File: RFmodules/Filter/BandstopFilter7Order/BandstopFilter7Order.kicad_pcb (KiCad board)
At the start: 2 copper layers, 26.8 x 9.2 mm, 17 parts, among them J1 SMA, J2 SMA

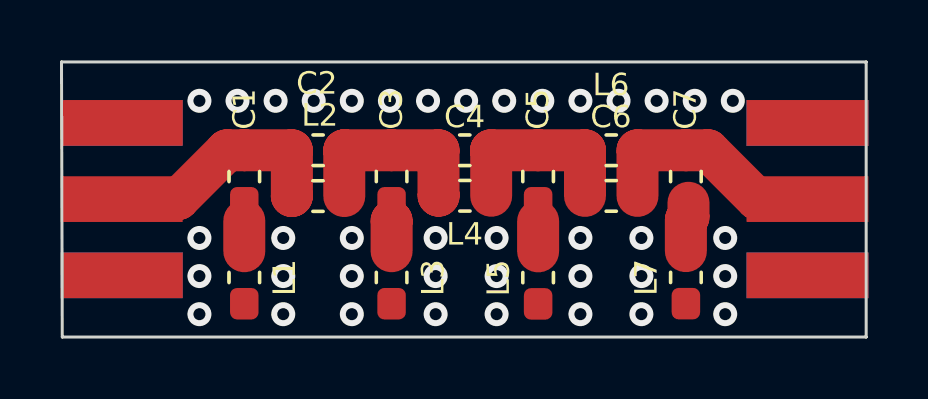
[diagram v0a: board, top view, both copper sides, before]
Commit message: Fix design guide issues
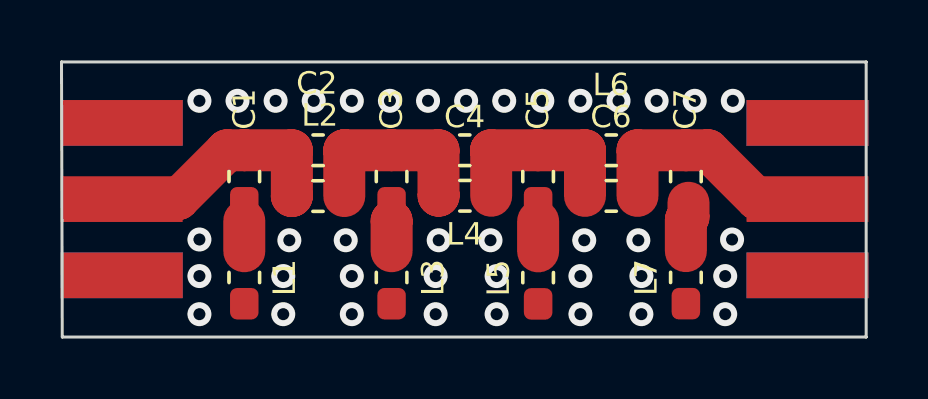
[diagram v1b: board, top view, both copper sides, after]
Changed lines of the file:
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@@
   (layers
     (0 F.Cu signal)
-    (31 B.Cu signal hide)
+    (31 B.Cu signal)
     (32 B.Adhes user)
     (33 F.Adhes user)
@@
     (last_trace_width 0.25)
     (trace_clearance 0.2)
-    (zone_clearance 0.2)
+    (zone_clearance 0.1)
     (zone_45_only no)
     (trace_min 0.2)
@@
   (gr_line (start 130.4798 96.2152) (end 130.4798 105.3846) (layer Edge.Cuts) (width 0.1))
   (gr_line (start 103.6574 96.2152) (end 130.4798 96.2152) (layer Edge.Cuts) (width 0.1))
-  (via (at 113.3348 102.0826) (size 0.8) (drill 0.4) (layers F.Cu B.Cu) (net 9))
-  (via (at 116.1288 102.0826) (size 0.8) (drill 0.4) (layers F.Cu B.Cu) (net 9))
-  (via (at 118.1608 102.0826) (size 0.8) (drill 0.4) (layers F.Cu B.Cu) (net 9))
-  (via (at 120.9548 102.0826) (size 0.8) (drill 0.4) (layers F.Cu B.Cu) (net 9))
-  (via (at 122.9868 102.0826) (size 0.8) (drill 0.4) (layers F.Cu B.Cu) (net 9))
-  (via (at 113.3348 104.6226) (size 0.8) (drill 0.4) (layers F.Cu B.Cu) (net 9))
-  (via (at 113.3348 103.3526) (size 0.8) (drill 0.4) (layers F.Cu B.Cu) (net 9))
-  (via (at 116.1288 103.3526) (size 0.8) (drill 0.4) (layers F.Cu B.Cu) (net 9))
-  (via (at 116.1288 104.6226) (size 0.8) (drill 0.4) (layers F.Cu B.Cu) (net 9))
-  (via (at 118.1608 103.3526) (size 0.8) (drill 0.4) (layers F.Cu B.Cu) (net 9))
-  (via (at 118.1608 104.6226) (size 0.8) (drill 0.4) (layers F.Cu B.Cu) (net 9))
-  (via (at 120.9548 103.3526) (size 0.8) (drill 0.4) (layers F.Cu B.Cu) (net 9))
-  (via (at 120.9548 104.6226) (size 0.8) (drill 0.4) (layers F.Cu B.Cu) (net 9))
-  (via (at 122.9868 103.3526) (size 0.8) (drill 0.4) (layers F.Cu B.Cu) (net 9))
-  (via (at 122.9868 104.6226) (size 0.8) (drill 0.4) (layers F.Cu B.Cu) (net 9))
-  (via (at 108.2548 103.3526) (size 0.8) (drill 0.4) (layers F.Cu B.Cu) (net 9))
-  (via (at 108.2548 102.0826) (size 0.8) (drill 0.4) (layers F.Cu B.Cu) (net 9))
-  (via (at 125.7808 102.0826) (size 0.8) (drill 0.4) (layers F.Cu B.Cu) (net 9))
-  (via (at 125.7808 103.3526) (size 0.8) (drill 0.4) (layers F.Cu B.Cu) (net 9))
-  (via (at 125.7808 104.6226) (size 0.8) (drill 0.4) (layers F.Cu B.Cu) (net 9))
-  (via (at 111.0488 104.6226) (size 0.8) (drill 0.4) (layers F.Cu B.Cu) (net 9))
-  (via (at 111.0488 103.3526) (size 0.8) (drill 0.4) (layers F.Cu B.Cu) (net 9))
-  (via (at 111.0488 102.0826) (size 0.8) (drill 0.4) (layers F.Cu B.Cu) (net 9))
   (segment (start 109.75086 99.15906) (end 111.33582 99.15906) (width 1.4) (layer F.Cu) (net 1) (status 30))
   (segment (start 111.33582 100.68312) (end 111.33334 100.6856) (width 1.4) (layer F.Cu) (net 1) (status 30))
@@
   (segment (start 124.47016 101.471737) (end 124.55721 101.384687) (width 1.4) (layer F.Cu) (net 8))
   (segment (start 124.47016 102.52202) (end 124.47016 101.471737) (width 1.4) (layer F.Cu) (net 8))
+  (via (at 113.1316 102.1588) (size 0.8) (drill 0.4) (layers F.Cu B.Cu) (net 9))
+  (via (at 116.2304 102.1588) (size 0.8) (drill 0.4) (layers F.Cu B.Cu) (net 9))
+  (via (at 117.9576 102.1588) (size 0.8) (drill 0.4) (layers F.Cu B.Cu) (net 9))
+  (via (at 121.0818 102.1588) (size 0.8) (drill 0.4) (layers F.Cu B.Cu) (net 9))
+  (via (at 122.8852 102.1588) (size 0.8) (drill 0.4) (layers F.Cu B.Cu) (net 9))
+  (via (at 113.3348 104.6226) (size 0.8) (drill 0.4) (layers F.Cu B.Cu) (net 9))
+  (via (at 113.3348 103.3526) (size 0.8) (drill 0.4) (layers F.Cu B.Cu) (net 9))
+  (via (at 116.1288 103.3526) (size 0.8) (drill 0.4) (layers F.Cu B.Cu) (net 9))
+  (via (at 116.1288 104.6226) (size 0.8) (drill 0.4) (layers F.Cu B.Cu) (net 9))
+  (via (at 118.1608 103.3526) (size 0.8) (drill 0.4) (layers F.Cu B.Cu) (net 9))
+  (via (at 118.1608 104.6226) (size 0.8) (drill 0.4) (layers F.Cu B.Cu) (net 9))
+  (via (at 120.9548 103.3526) (size 0.8) (drill 0.4) (layers F.Cu B.Cu) (net 9))
+  (via (at 120.9548 104.6226) (size 0.8) (drill 0.4) (layers F.Cu B.Cu) (net 9))
+  (via (at 122.9868 103.3526) (size 0.8) (drill 0.4) (layers F.Cu B.Cu) (net 9))
+  (via (at 122.9868 104.6226) (size 0.8) (drill 0.4) (layers F.Cu B.Cu) (net 9))
+  (via (at 108.2548 103.3526) (size 0.8) (drill 0.4) (layers F.Cu B.Cu) (net 9))
+  (via (at 108.2548 102.1334) (size 0.8) (drill 0.4) (layers F.Cu B.Cu) (net 9))
+  (via (at 126.0094 102.1334) (size 0.8) (drill 0.4) (layers F.Cu B.Cu) (net 9))
+  (via (at 125.7808 103.3526) (size 0.8) (drill 0.4) (layers F.Cu B.Cu) (net 9))
+  (via (at 125.7808 104.6226) (size 0.8) (drill 0.4) (layers F.Cu B.Cu) (net 9))
+  (via (at 111.0488 104.6226) (size 0.8) (drill 0.4) (layers F.Cu B.Cu) (net 9))
+  (via (at 111.0488 103.3526) (size 0.8) (drill 0.4) (layers F.Cu B.Cu) (net 9))
+  (via (at 111.252 102.1588) (size 0.8) (drill 0.4) (layers F.Cu B.Cu) (net 9))
   (via (at 108.2548 97.5106) (size 0.8) (drill 0.4) (layers F.Cu B.Cu) (net 9))
   (via (at 109.5248 97.5106) (size 0.8) (drill 0.4) (layers F.Cu B.Cu) (net 9))
@@
   (via (at 108.2548 104.6226) (size 0.8) (drill 0.4) (layers F.Cu B.Cu) (net 9))
   (zone (net 9) (net_name GND) (layer F.Cu) (hatch edge 0.508)
-    (connect_pads yes (clearance 0.2))
+    (connect_pads yes (clearance 0.1))
     (min_thickness 0.254)
     (fill yes (arc_segments 16) (thermal_gap 0.508) (thermal_bridge_width 0.508))
@@
   )
   (zone (net 9) (net_name GND) (layer B.Cu) (hatch edge 0.508)
-    (connect_pads yes (clearance 0.2))
+    (connect_pads yes (clearance 0.1))
     (min_thickness 0.254)
     (fill yes (arc_segments 16) (thermal_gap 0.508) (thermal_bridge_width 0.508))

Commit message: Fix typos
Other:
- board text added: "Bandstop Filter 7th Order Revision 0.1.0 - 01/2019"
- board text removed: "Bandstop Filter 7 Order Revision 0.1.0 - 01/2019"
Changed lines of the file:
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@@
     (32 B.Adhes user)
     (33 F.Adhes user)
-    (34 B.Paste user hide)
+    (34 B.Paste user)
     (35 F.Paste user)
-    (36 B.SilkS user hide)
-    (37 F.SilkS user hide)
+    (36 B.SilkS user)
+    (37 F.SilkS user)
     (38 B.Mask user)
     (39 F.Mask user)
@@
     (47 F.CrtYd user)
     (48 B.Fab user)
-    (49 F.Fab user hide)
+    (49 F.Fab user)
   )
   (setup
@@
     (effects (font (size 0.75 0.75) (thickness 0.1875)) (justify mirror))
   )
-  (gr_text "Bandstop Filter 7 Order\nRevision 0.1.0 - 01/2019" (at 125.81128 97.82556) (layer B.SilkS)
+  (gr_text "Bandstop Filter 7th Order\nRevision 0.1.0 - 01/2019" (at 125.81128 97.82556) (layer B.SilkS)
     (effects (font (size 0.75 0.75) (thickness 0.1875)) (justify left mirror))
   )

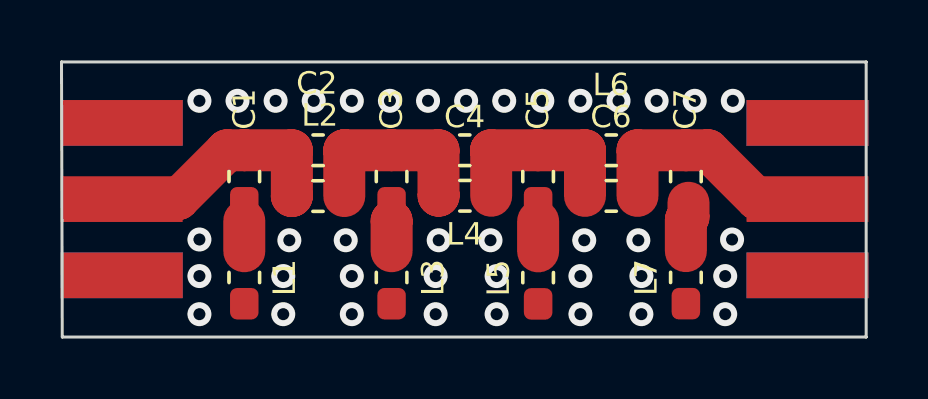
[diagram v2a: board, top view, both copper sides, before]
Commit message: Update board descriptions, add Bandstop elliptic filter 5th order
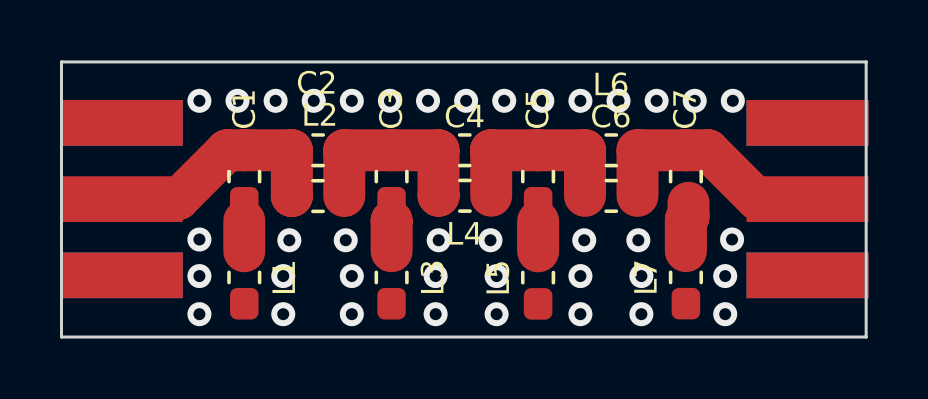
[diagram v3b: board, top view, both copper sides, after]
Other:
- board text added: "Bandstop Filter 7th Order Revision 1 - 01/2019"
- board text removed: "Bandstop Filter 7th Order Revision 0.1.0 - 01/2019"
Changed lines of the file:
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@@
     (solder_mask_min_width 0.25)
     (aux_axis_origin 0 0)
-    (grid_origin 103.6828 105.3846)
+    (grid_origin 103.6574 105.3846)
     (visible_elements FFFFFF7F)
     (pcbplotparams
@@
     (effects (font (size 0.75 0.75) (thickness 0.1875)) (justify mirror))
   )
-  (gr_text "Bandstop Filter 7th Order\nRevision 0.1.0 - 01/2019" (at 125.81128 97.82556) (layer B.SilkS)
+  (gr_text "Bandstop Filter 7th Order\nRevision 1 - 01/2019" (at 125.81128 97.82556) (layer B.SilkS)
     (effects (font (size 0.75 0.75) (thickness 0.1875)) (justify left mirror))
   )
-  (gr_line (start 103.6828 105.3846) (end 103.6574 96.2152) (layer Edge.Cuts) (width 0.1))
-  (gr_line (start 130.4798 105.3846) (end 103.6828 105.3846) (layer Edge.Cuts) (width 0.1))
+  (gr_line (start 103.6574 105.3846) (end 103.6574 96.2152) (layer Edge.Cuts) (width 0.1))
+  (gr_line (start 130.4798 105.3846) (end 103.6574 105.3846) (layer Edge.Cuts) (width 0.1))
   (gr_line (start 130.4798 96.2152) (end 130.4798 105.3846) (layer Edge.Cuts) (width 0.1))
   (gr_line (start 103.6574 96.2152) (end 130.4798 96.2152) (layer Edge.Cuts) (width 0.1))
@@
     (polygon
       (pts
-        (xy 103.6574 96.2152) (xy 130.4798 96.2152) (xy 130.4798 105.3846) (xy 103.759 105.3846) (xy 103.6828 105.3846)
+        (xy 103.6574 96.2152) (xy 130.4798 96.2152) (xy 130.4798 105.3846) (xy 103.759 105.3846) (xy 103.6574 105.3846)
       )
     )
@@
     (polygon
       (pts
-        (xy 130.4798 105.3846) (xy 103.6828 105.3846) (xy 103.6574 96.2152) (xy 130.4798 96.2152)
+        (xy 130.4798 105.3846) (xy 103.6574 105.3846) (xy 103.6574 96.2152) (xy 130.4798 96.2152)
       )
     )
